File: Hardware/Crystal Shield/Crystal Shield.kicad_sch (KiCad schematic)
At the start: 38 parts, among them J1 USB_B_Micro, U1 AP63205WU, U2 NCP1117-3.3_SOT223, U3 ESP32-C3-WROOM-02, U4 TXS0102DCT, U5 TXS0108EPW

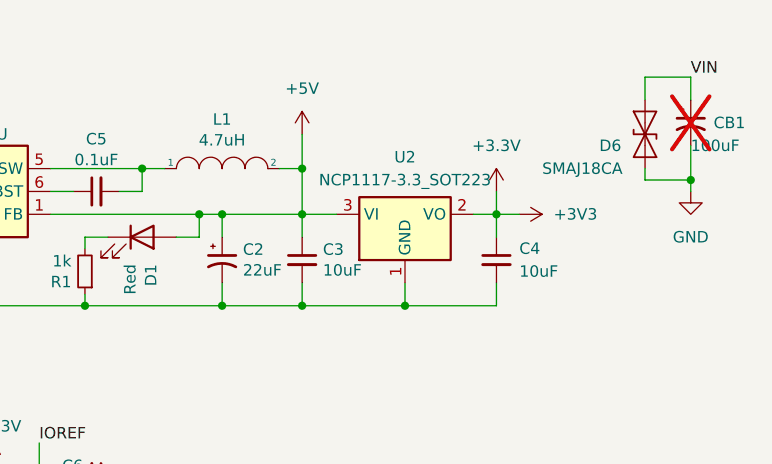
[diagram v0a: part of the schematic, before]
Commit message: BOM fix, replace NCP1117 with TLV1117 and add Arduino stacking headers
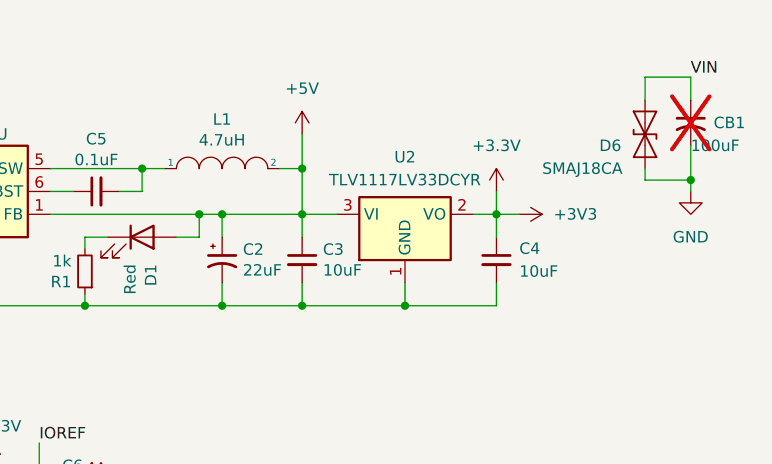
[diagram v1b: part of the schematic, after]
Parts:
- A1: MFG (none) -> Adafruit; PN (none) -> 85
- U2: value NCP1117-3.3_SOT223 -> TLV1117LV33DCYR; MFG ONSemi -> Texas Insturments; PN NCP1117ST33T3G -> TLV1117LV33DCYR
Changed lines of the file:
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@@
       (effects (font (size 1.27 1.27)))
     )
-    (property "Value" "NCP1117-3.3_SOT223" (at 228.6 31.75 0)
+    (property "Value" "TLV1117LV33DCYR" (at 228.6 31.75 0)
       (effects (font (size 1.27 1.27)))
     )
@@
       (effects (font (size 1.27 1.27)) hide)
     )
-    (property "Datasheet" "http://www.onsemi.com/pub_link/Collateral/NCP1117-D.PDF" (at 231.14 41.91 0)
-      (effects (font (size 1.27 1.27)) hide)
-    )
-    (property "MFG" "ONSemi" (at 228.6 35.56 0)
-      (effects (font (size 1.27 1.27)) hide)
-    )
-    (property "PN" "NCP1117ST33T3G" (at 228.6 35.56 0)
+    (property "Datasheet" "https://www.ti.com/lit/gpn/tlv1117lv" (at 231.14 41.91 0)
+      (effects (font (size 1.27 1.27)) hide)
+    )
+    (property "MFG" "Texas Insturments" (at 228.6 35.56 0)
+      (effects (font (size 1.27 1.27)) hide)
+    )
+    (property "PN" "TLV1117LV33DCYR" (at 228.6 35.56 0)
       (effects (font (size 1.27 1.27)) hide)
     )
@@
       (effects (font (size 1.27 1.27)) hide)
     )
+    (property "MFG" "Adafruit" (at 34.29 166.37 0)
+      (effects (font (size 1.27 1.27)) hide)
+    )
+    (property "PN" "85" (at 34.29 166.37 0)
+      (effects (font (size 1.27 1.27)) hide)
+    )
